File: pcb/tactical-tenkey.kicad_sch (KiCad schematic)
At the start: 46 parts, among them J1 io_side, J2 esp32_side, J3 OLED, Q2 FS8205, SW1 SW_SPDT, U1 XIAO-ESP32-S3-SMD, U2 DW01A

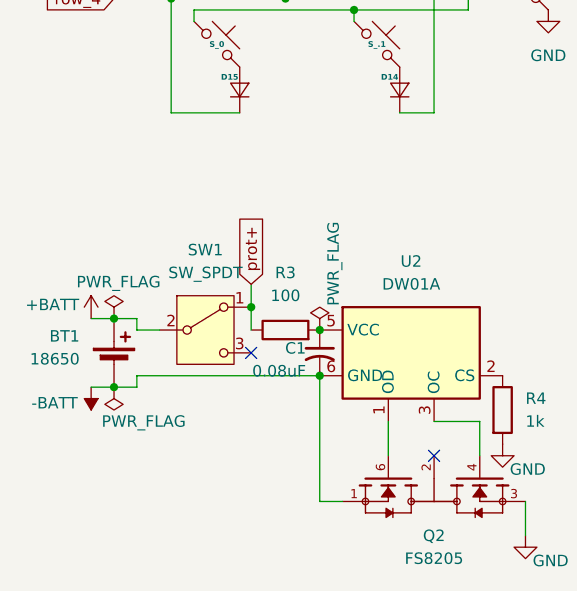
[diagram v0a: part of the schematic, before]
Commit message: fix battery mgmt not working after switching off
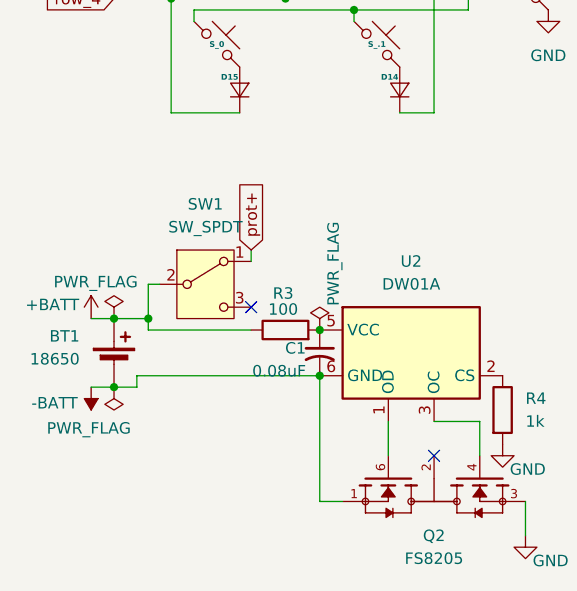
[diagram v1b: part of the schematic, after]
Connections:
- net +BATT: now also R3.1
- net prot+: no longer R3.1
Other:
- moved on the sheet: SW1
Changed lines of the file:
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@@
 	)
 	(junction
+		(at 82.55 144.78)
+		(diameter 0)
+		(color 0 0 0 0)
+	)
+	(junction
 		(at 97.79 96.52)
 		(diameter 0)
@@
 		(color 0 0 0 0)
 	)
-	(junction
-		(at 93.98 143.51)
-		(diameter 0)
-		(color 0 0 0 0)
-	)
 	(no_connect
 		(at 184.15 60.96)
 	)
 	(no_connect
-		(at 93.98 148.59)
+		(at 93.98 143.51)
 	)
 	(no_connect
@@
 	(wire
 		(pts
+			(xy 93.98 146.05) (xy 82.55 146.05)
+		)
+		(stroke
+			(width 0)
+			(type default)
+		)
+	)
+	(wire
+		(pts
 			(xy 109.22 160.02) (xy 109.22 156.21)
 		)
@@
 	(wire
 		(pts
-			(xy 81.28 146.05) (xy 81.28 144.78)
-		)
-		(stroke
-			(width 0)
-			(type default)
-		)
-	)
-	(wire
-		(pts
 			(xy 78.74 96.52) (xy 85.09 96.52)
 		)
@@
 	(wire
 		(pts
+			(xy 82.55 146.05) (xy 82.55 144.78)
+		)
+		(stroke
+			(width 0)
+			(type default)
+		)
+	)
+	(wire
+		(pts
 			(xy 177.8 135.89) (xy 177.8 142.24)
 		)
@@
 	(wire
 		(pts
-			(xy 81.28 144.78) (xy 78.74 144.78)
+			(xy 82.55 140.97) (xy 83.82 140.97)
 		)
 		(stroke
@@
 	(wire
 		(pts
-			(xy 93.98 140.97) (xy 93.98 143.51)
+			(xy 93.98 137.16) (xy 93.98 138.43)
 		)
 		(stroke
@@
 	(wire
 		(pts
-			(xy 154.94 90.17) (xy 163.83 90.17)
+			(xy 82.55 144.78) (xy 78.74 144.78)
 		)
 		(stroke
@@
 	(wire
 		(pts
-			(xy 179.07 134.62) (xy 179.07 144.78)
+			(xy 154.94 90.17) (xy 163.83 90.17)
 		)
 		(stroke
@@
 	(wire
 		(pts
-			(xy 83.82 146.05) (xy 81.28 146.05)
+			(xy 179.07 134.62) (xy 179.07 144.78)
 		)
 		(stroke
@@
 	(wire
 		(pts
-			(xy 118.11 60.96) (xy 118.11 80.01)
+			(xy 82.55 140.97) (xy 82.55 144.78)
 		)
 		(stroke
@@
 	(wire
 		(pts
-			(xy 76.2 144.78) (xy 78.74 144.78)
+			(xy 118.11 60.96) (xy 118.11 80.01)
 		)
 		(stroke
@@
 	(wire
 		(pts
-			(xy 116.84 83.82) (xy 116.84 90.17)
+			(xy 76.2 144.78) (xy 78.74 144.78)
 		)
 		(stroke
@@
 	(wire
 		(pts
-			(xy 154.94 46.99) (xy 154.94 90.17)
+			(xy 116.84 83.82) (xy 116.84 90.17)
 		)
 		(stroke
@@
 	(wire
 		(pts
-			(xy 93.98 143.51) (xy 93.98 146.05)
+			(xy 154.94 46.99) (xy 154.94 90.17)
 		)
 		(stroke
@@
 	(global_label "prot+"
 		(shape input)
-		(at 93.98 140.97 90)
+		(at 93.98 137.16 90)
 		(fields_autoplaced yes)
 		(effects
@@
 		)
 		(property "Intersheetrefs" "${INTERSHEET_REFS}"
-			(at 93.98 132.6025 90)
+			(at 93.98 128.7925 90)
 			(effects
 				(font
@@
 		(on_board yes)
 		(dnp no)
-		(fields_autoplaced yes)
 		(property "Reference" "R3"
-			(at 97.79 139.7 90)
+			(at 97.536 141.986 90)
 			(effects
 				(font
@@
 		)
 		(property "Value" "100"
-			(at 97.79 142.24 90)
+			(at 97.536 143.764 90)
 			(effects
 				(font
@@
 		)
 		(property "Value" "PWR_FLAG"
-			(at 79.248 140.716 0)
+			(at 76.708 140.716 0)
 			(effects
 				(font
@@
 	(symbol
 		(lib_id "Switch:SW_SPDT")
-		(at 88.9 146.05 0)
+		(at 88.9 140.97 0)
 		(unit 1)
 		(exclude_from_sim no)
@@
 		(fields_autoplaced yes)
 		(property "Reference" "SW1"
-			(at 88.9 137.16 0)
+			(at 88.9 132.08 0)
 			(effects
 				(font
@@
 		)
 		(property "Value" "SW_SPDT"
-			(at 88.9 139.7 0)
+			(at 88.9 134.62 0)
 			(effects
 				(font
@@
 		)
 		(property "Footprint" "Personal:SS-12F23G5"
-			(at 88.9 146.05 0)
+			(at 88.9 140.97 0)
 			(effects
 				(font
@@
 		)
 		(property "Datasheet" "~"
-			(at 88.9 153.67 0)
+			(at 88.9 148.59 0)
 			(effects
 				(font
@@
 		)
 		(property "Description" "Switch, single pole double throw"
-			(at 88.9 146.05 0)
+			(at 88.9 140.97 0)
 			(effects
 				(font
@@
 		)
 		(property "Value" "PWR_FLAG"
-			(at 82.042 156.21 0)
+			(at 75.946 156.972 0)
 			(effects
 				(font
